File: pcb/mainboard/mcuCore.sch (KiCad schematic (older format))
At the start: 2 parts

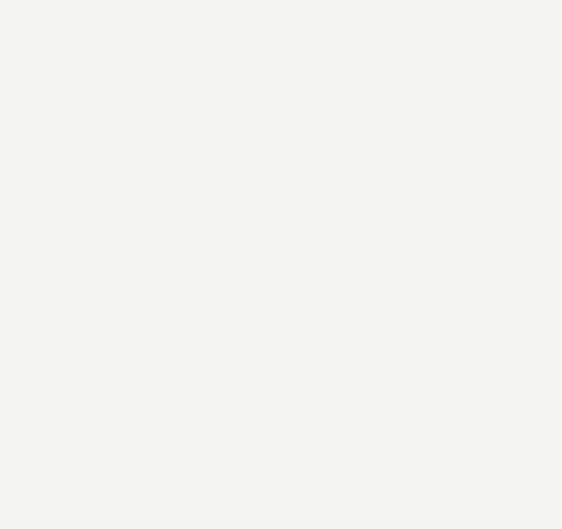
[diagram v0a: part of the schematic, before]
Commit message: worked on PoE regulator
Added the SRAM
Added an EEPROM and a FLASH as nonvolatileMemory
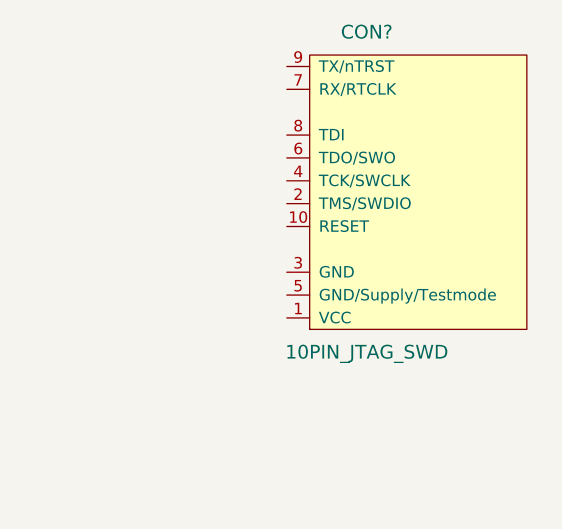
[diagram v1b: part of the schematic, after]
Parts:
- added CON?: 10PIN_JTAG_SWD, symbol 10PIN_JTAG_SWD
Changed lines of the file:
@@
 $Descr A4 11693 8268
 encoding utf-8
-Sheet 4 9
-Title ""
+Sheet 3 10
+Title "ProzEthernatorMainboard"
 Date ""
-Rev ""
-Comp ""
+Rev "00"
+Comp "Shimatta"
 Comment1 ""
 Comment2 ""
@@
 	1    0    0    -1
 $EndComp
+$Comp
+L 10PIN_JTAG_SWD CON?
+U 1 1 5A86049C
+P 10250 1350
+F 0 "CON?" H 10150 650 60  0000 C CNN
+F 1 "10PIN_JTAG_SWD" H 10150 2050 60  0000 C CNN
+F 2 "" H 10250 1350 60  0001 C CNN
+F 3 "" H 10250 1350 60  0001 C CNN
+	1    10250 1350
+	-1   0    0    1
+$EndComp
 $EndSCHEMATC
